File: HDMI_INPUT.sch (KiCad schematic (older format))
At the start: 52 parts, among them J1 HDMI_A, U1 TPD4S010DQAR, U2 TPD4S010DQAR, U3 ABM3B-24.000MHZ-B2-T, U4 TPS2061, U5 ADV7611

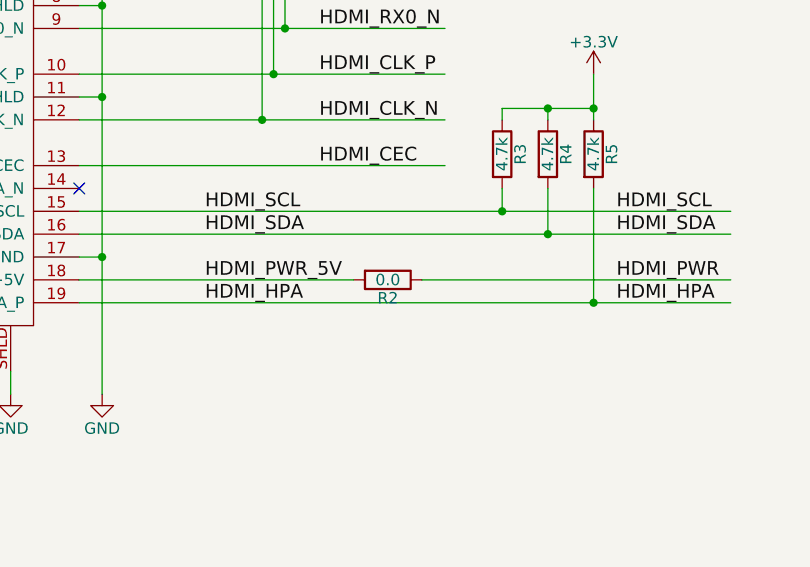
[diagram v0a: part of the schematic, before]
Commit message: Hdmi and RGB is routed, waiting for trace matching
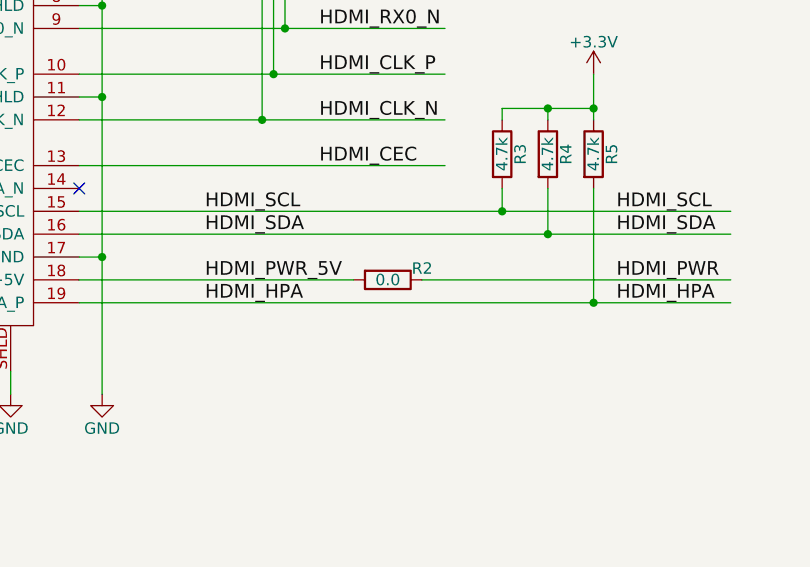
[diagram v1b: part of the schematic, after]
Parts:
- U1, U2: footprint (none) -> misc:10-USON
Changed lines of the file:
@@
 U 1 1 56F8ACED
 P 5350 5200
-F 0 "R2" V 5430 5200 50  0000 C CNN
+F 0 "R2" V 5300 5350 50  0000 C CNN
 F 1 "0.0" V 5350 5200 50  0000 C CNN
 F 2 "Resistors_SMD:R_0402" V 5280 5200 30  0001 C CNN
@@
 F 0 "U2" H 5500 2750 60  0000 C CNN
 F 1 "TPD4S010DQAR" H 5650 1800 60  0000 C CNN
-F 2 "" H 5550 2800 60  0001 C CNN
+F 2 "misc:10-USON" H 5550 2800 60  0001 C CNN
 F 3 "" H 5550 2800 60  0000 C CNN
 	1    5650 2300
@@
 F 0 "U1" H 5500 1600 60  0000 C CNN
 F 1 "TPD4S010DQAR" H 5650 650 60  0000 C CNN
-F 2 "" H 5550 1650 60  0001 C CNN
+F 2 "misc:10-USON" H 5550 1650 60  0001 C CNN
 F 3 "" H 5550 1650 60  0000 C CNN
 	1    5650 1150

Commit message: Basic layout of all components on PCB
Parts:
- U3: footprint (none) -> SMD_Packages:XTAL_ABRACON
- U4: footprint (none) -> TO_SOT_Packages_SMD:SOT-23-5
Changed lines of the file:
@@
 F 0 "U4" H 8050 7700 60  0000 C CNN
 F 1 "TPS2061" H 8300 7300 60  0000 C CNN
-F 2 "" H 8250 7450 60  0001 C CNN
+F 2 "TO_SOT_Packages_SMD:SOT-23-5" H 8250 7450 60  0001 C CNN
 F 3 "" H 8250 7450 60  0000 C CNN
 F 4 "http://www.mouser.com/ProductDetail/Texas-Instruments/TPS2061CDBVT/?qs=sGAEpiMZZMuCmTIBzycWfA%2fkltuuzBRGGymV4N3jSG0%3d" H 8350 8000 60  0001 C CNN "Link"
@@
 F 0 "U3" H 8000 4050 60  0000 C CNN
 F 1 "ABM3B-24.000MHZ-B2-T" H 8200 3950 60  0000 C CNN
-F 2 "" H 7850 3550 60  0001 C CNN
+F 2 "SMD_Packages:XTAL_ABRACON" H 7850 3550 60  0001 C CNN
 F 3 "" H 7950 3650 60  0000 C CNN
 F 4 "ABM3B-24.000MHZ-B2-T" H 8050 3450 60  0001 C CNN "Part #"

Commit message: Routing power, changed buttons connections, and a few pther connections
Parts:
- U5: footprint ADV7611:LQFP-64_TH_10x10mm_Pitch0.5mm -> misc:LQFP-64_TH_10x10mm_Pitch0.5mm
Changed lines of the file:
@@
 F 0 "U5" H 11550 3400 50  0000 C CNN
 F 1 "ADV7611" H 11550 3600 50  0000 C CNN
-F 2 "ADV7611:LQFP-64_TH_10x10mm_Pitch0.5mm" H 11550 3500 50  0001 C CNN
+F 2 "misc:LQFP-64_TH_10x10mm_Pitch0.5mm" H 11550 3500 50  0001 C CNN
 F 3 "DOCUMENTATION" H 11550 3500 50  0001 C CNN
 	1    11550 3500

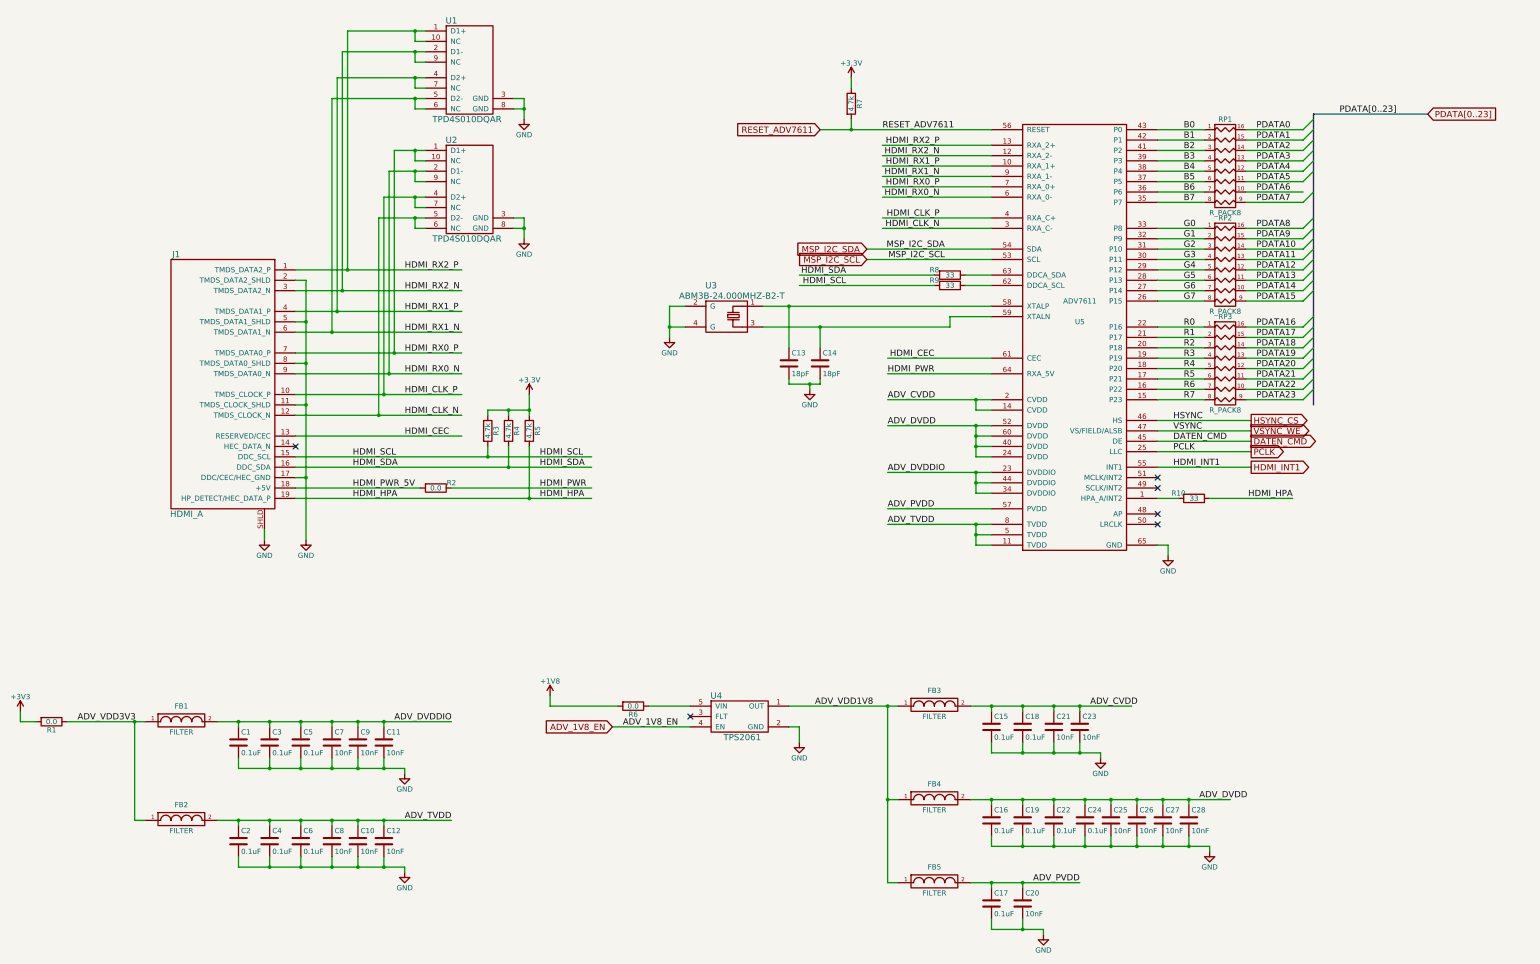
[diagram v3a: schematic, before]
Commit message: Schematic Titles
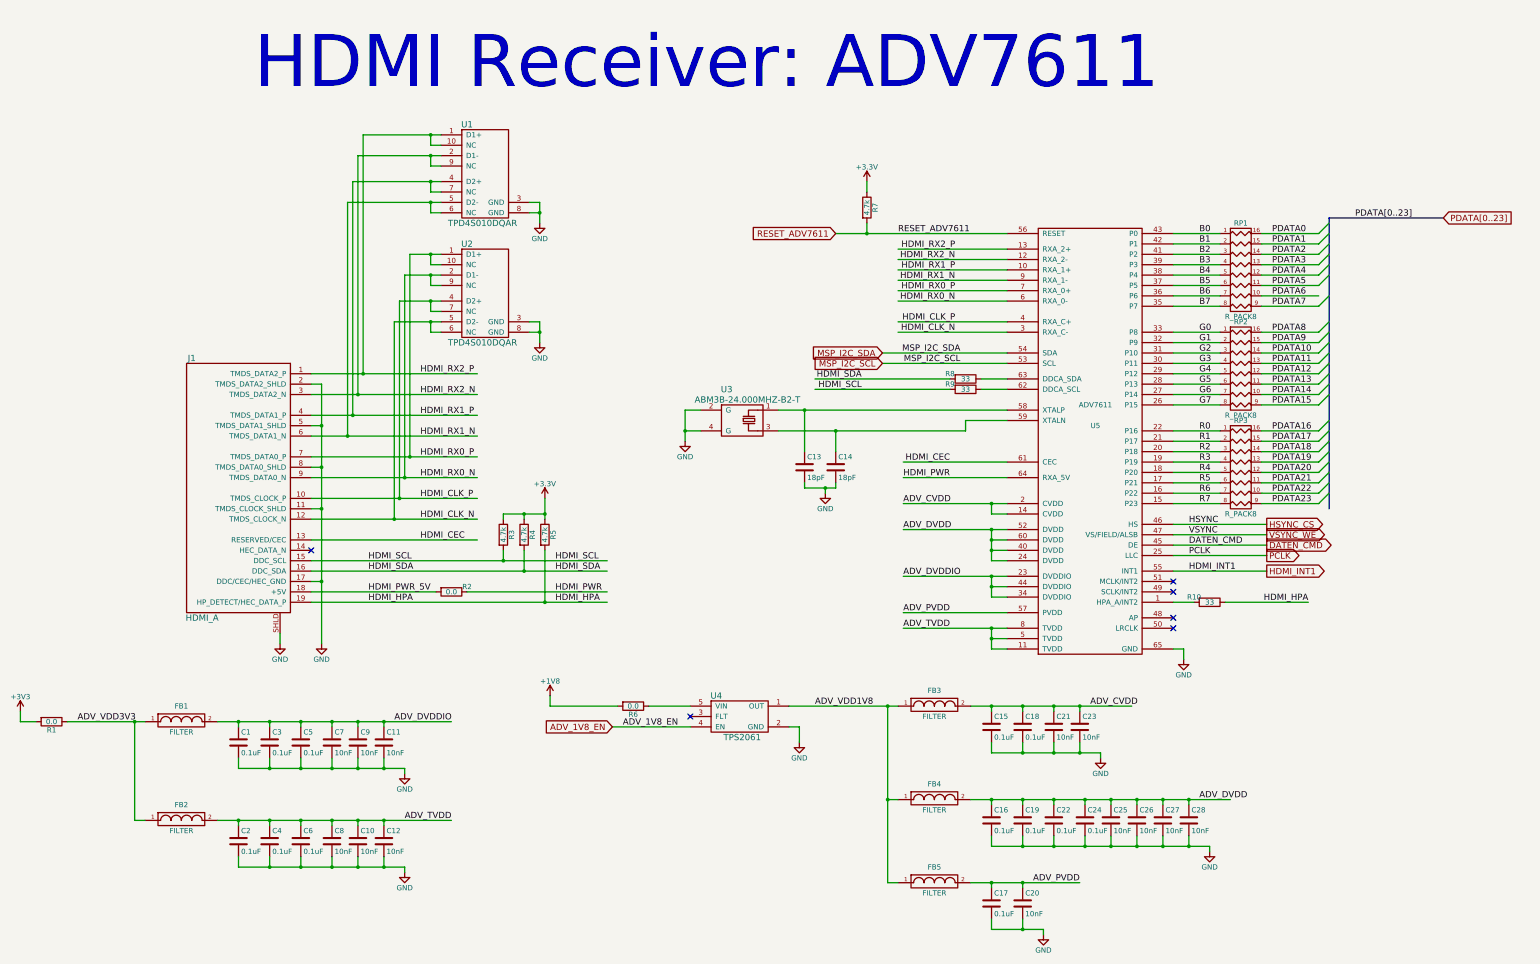
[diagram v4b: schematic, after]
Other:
- note added: "HDMI Receiver: ADV7611"
- moved on the sheet: C13, C14, J1, R10, R2, R3, R4, R5, R7, R8, R9, RP1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

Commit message: Changed BOM for several components
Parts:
- J1: Cost (none) -> 0.73; Link (none) -> http://www.mouser.com/ProductDetail/FCI/10029449-111RLF/?qs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; Part # (none) -> 10029449-111RLF; Supplier (none) -> Mouser
- RP1, RP2: Cost (none) -> .31; Link (none) -> http://www.mouser.com/ProductDetail/Yageo/YC248-JR-0733RL/?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; Part # (none) -> YC248-JR-0733RL; Supplier (none) -> Mouser
- RP3: Cost (none) -> 0.31; Link (none) -> http://www.mouser.com/ProductDetail/Yageo/YC248-JR-0733RL/?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; Part # (none) -> YC248-JR-0733RL; Supplier (none) -> Mouser
- U1: Cost (none) -> 0.66; Link (none) -> http://www.mouser.com/ProductDetail/Texas-Instruments/TPD4S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; Part # (none) -> TPD4S010DQAR; Supplier (none) -> Mouser
- U2: Cost (none) -> .66; Link (none) -> http://www.mouser.com/ProductDetail/Texas-Instruments/TPD4S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; Part # (none) -> TPD4S010DQAR; Supplier (none) -> Mouser
- U4: Cost (none) -> 1.48
- U5: Cost (none) -> 14.21; Link (none) -> http://www.mouser.com/ProductDetail/Analog-Devices/ADV7611B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; Part # (none) -> ADV7611BSWZ-P; Supplier (none) -> Mouser
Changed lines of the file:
@@
 F 2 "hdmi:FCI_10029449-11[13]RLF" H 2950 4700 60  0001 C CNN
 F 3 "" H 2950 4700 60  0000 C CNN
+F 4 "10029449-111RLF" H 3450 5200 60  0001 C CNN "Part #"
+F 5 "0.73" H 3450 5200 60  0001 C CNN "Cost"
+F 6 "http://www.mouser.com/ProductDetail/FCI/10029449-111RLF/?qs=sGAEpiMZZMtAYTMy7wxAr9LCvXDZCuSkPfr%252b91JPIb8%3d" H 3450 5200 60  0001 C CNN "Link"
+F 7 "Mouser" H 3450 5200 60  0001 C CNN "Supplier"
 	1    3450 5200
 	-1   0    0    -1
@@
 F 2 "misc:LQFP-64_TH_10x10mm_Pitch0.5mm" H 11700 4500 50  0001 C CNN
 F 3 "DOCUMENTATION" H 11700 4500 50  0001 C CNN
+F 4 "ADV7611BSWZ-P" H 11700 4500 60  0001 C CNN "Part #"
+F 5 "14.21" H 11700 4500 60  0001 C CNN "Cost"
+F 6 "http://www.mouser.com/ProductDetail/Analog-Devices/ADV7611BSWZ-P/?qs=sGAEpiMZZMv9Q1JI0Mo%2ftQPxLbY1tPB%252b" H 11700 4500 60  0001 C CNN "Link"
+F 7 "Mouser" H 11700 4500 60  0001 C CNN "Supplier"
 	1    11700 4500
 	1    0    0    -1
@@
 F 2 "rpack:RPACK-8_0616" H 13100 3100 60  0001 C CNN
 F 3 "" H 13100 3100 60  0000 C CNN
+F 4 "YC248-JR-0733RL" H 13100 3100 60  0001 C CNN "Part #"
+F 5 ".31" H 13100 3100 60  0001 C CNN "Cost"
+F 6 "http://www.mouser.com/ProductDetail/Yageo/YC248-JR-0733RL/?qs=%2fha2pyFadujrU2xFewWLBkAmO3yjJR9q5AB4Bh4PJQzwmQRmZIRzCA%3d%3d" H 13100 3100 60  0001 C CNN "Link"
+F 7 "Mouser" H 13100 3100 60  0001 C CNN "Supplier"
 	1    13100 3100
 	1    0    0    -1
@@
 F 2 "rpack:RPACK-8_0616" H 13100 4050 60  0001 C CNN
 F 3 "" H 13100 4050 60  0000 C CNN
+F 4 "YC248-JR-0733RL" H 13100 4050 60  0001 C CNN "Part #"
+F 5 ".31" H 13100 4050 60  0001 C CNN "Cost"
+F 6 "http://www.mouser.com/ProductDetail/Yageo/YC248-JR-0733RL/?qs=%2fha2pyFadujrU2xFewWLBkAmO3yjJR9q5AB4Bh4PJQzwmQRmZIRzCA%3d%3d" H 13100 4050 60  0001 C CNN "Link"
+F 7 "Mouser" H 13100 4050 60  0001 C CNN "Supplier"
 	1    13100 4050
 	1    0    0    -1
@@
 F 2 "rpack:RPACK-8_0616" H 13100 5000 60  0001 C CNN
 F 3 "" H 13100 5000 60  0000 C CNN
+F 4 "YC248-JR-0733RL" H 13100 5000 60  0001 C CNN "Part #"
+F 5 "0.31" H 13100 5000 60  0001 C CNN "Cost"
+F 6 "http://www.mouser.com/ProductDetail/Yageo/YC248-JR-0733RL/?qs=%2fha2pyFadujrU2xFewWLBkAmO3yjJR9q5AB4Bh4PJQzwmQRmZIRzCA%3d%3d" H 13100 5000 60  0001 C CNN "Link"
+F 7 "Mouser" H 13100 5000 60  0001 C CNN "Supplier"
 	1    13100 5000
 	1    0    0    -1
@@
 F 2 "TO_SOT_Packages_SMD:SOT-23-5" H 8250 7450 60  0001 C CNN
 F 3 "" H 8250 7450 60  0000 C CNN
-F 4 "http://www.mouser.com/ProductDetail/Texas-Instruments/TPS2061CDBVT/?qs=sGAEpiMZZMuCmTIBzycWfA%2fkltuuzBRGGymV4N3jSG0%3d" H 8350 8000 60  0001 C CNN "Link"
-F 5 "TPS2061CDBVT" H 8150 7800 60  0001 C CNN "Part #"
+F 4 "TPS2061CDBVT" H 8150 7800 60  0001 C CNN "Part #"
+F 5 "1.48" H 8250 7450 60  0001 C CNN "Cost"
+F 6 "http://www.mouser.com/ProductDetail/Texas-Instruments/TPS2061CDBVT/?qs=sGAEpiMZZMuCmTIBzycWfA%2fkltuuzBRGGymV4N3jSG0%3d" H 8350 8000 60  0001 C CNN "Link"
 	1    8250 7450
 	1    0    0    -1
@@
 F 2 "misc:10-USON" H 5700 3800 60  0001 C CNN
 F 3 "" H 5700 3800 60  0000 C CNN
+F 4 "TPD4S010DQAR" H 5800 3300 60  0001 C CNN "Part #"
+F 5 ".66" H 5800 3300 60  0001 C CNN "Cost"
+F 6 "http://www.mouser.com/ProductDetail/Texas-Instruments/TPD4S010DQAR/?qs=%2fha2pyFadujvqJsP1FaVJ5cYodIGUpQ4CFN5UL%2fXzLhaigQuhTlVpA%3d%3d" H 5800 3300 60  0001 C CNN "Link"
+F 7 "Mouser" H 5800 3300 60  0001 C CNN "Supplier"
 	1    5800 3300
 	1    0    0    -1
@@
 F 2 "misc:10-USON" H 5700 2650 60  0001 C CNN
 F 3 "" H 5700 2650 60  0000 C CNN
+F 4 "TPD4S010DQAR" H 5800 2150 60  0001 C CNN "Part #"
+F 5 "0.66" H 5800 2150 60  0001 C CNN "Cost"
+F 6 "http://www.mouser.com/ProductDetail/Texas-Instruments/TPD4S010DQAR/?qs=%2fha2pyFadujvqJsP1FaVJ5cYodIGUpQ4CFN5UL%2fXzLhaigQuhTlVpA%3d%3d" H 5800 2150 60  0001 C CNN "Link"
+F 7 "Mouser" H 5800 2150 60  0001 C CNN "Supplier"
 	1    5800 2150
 	1    0    0    -1
